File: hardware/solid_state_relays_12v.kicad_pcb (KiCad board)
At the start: 2 copper layers, 100 x 90 mm, 86 parts, among them J1 1190297, J2 1190297, J3 1190297, J4 1190297, J5 1190297, J6 1190297, J7 1190297, J8 1190297, Q1 IRF4905PBF, Q2 IRF4905PBF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

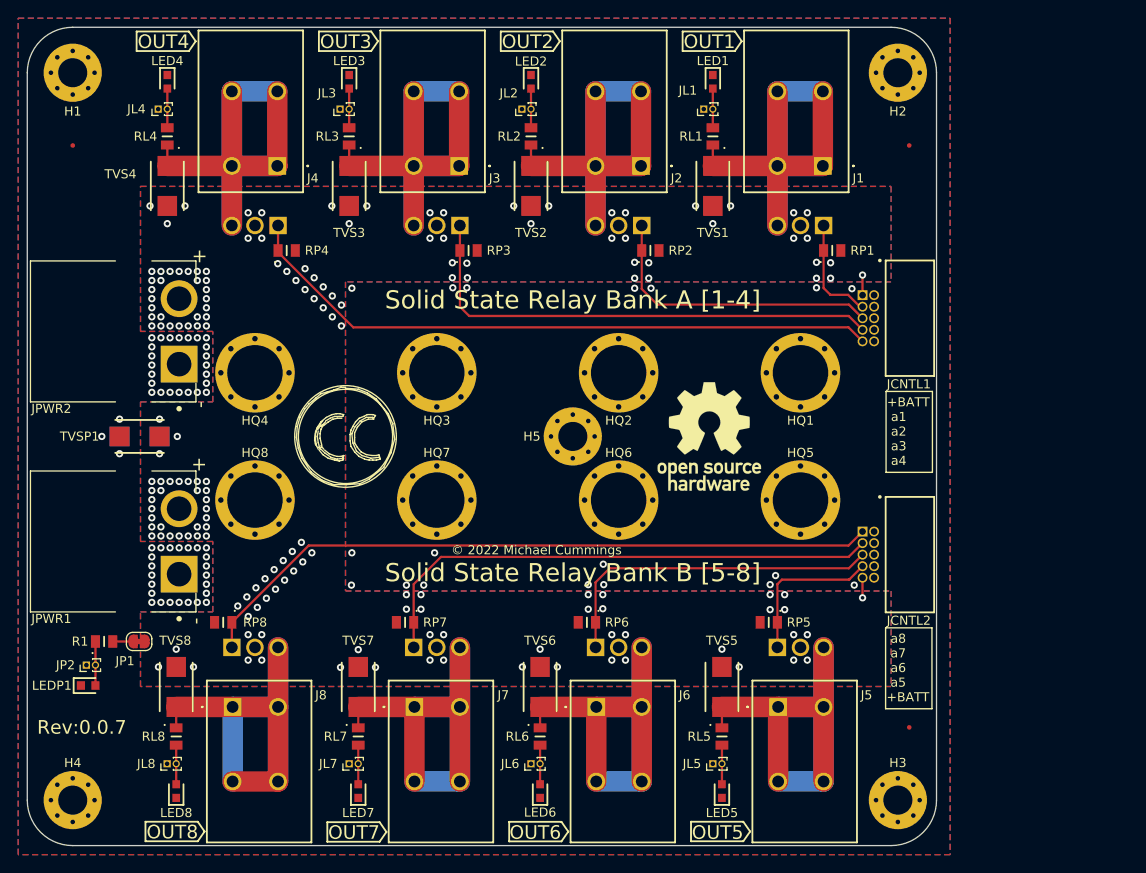
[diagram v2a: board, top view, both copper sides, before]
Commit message: Misc updates mostly related to Silkscreen and adding draft production output
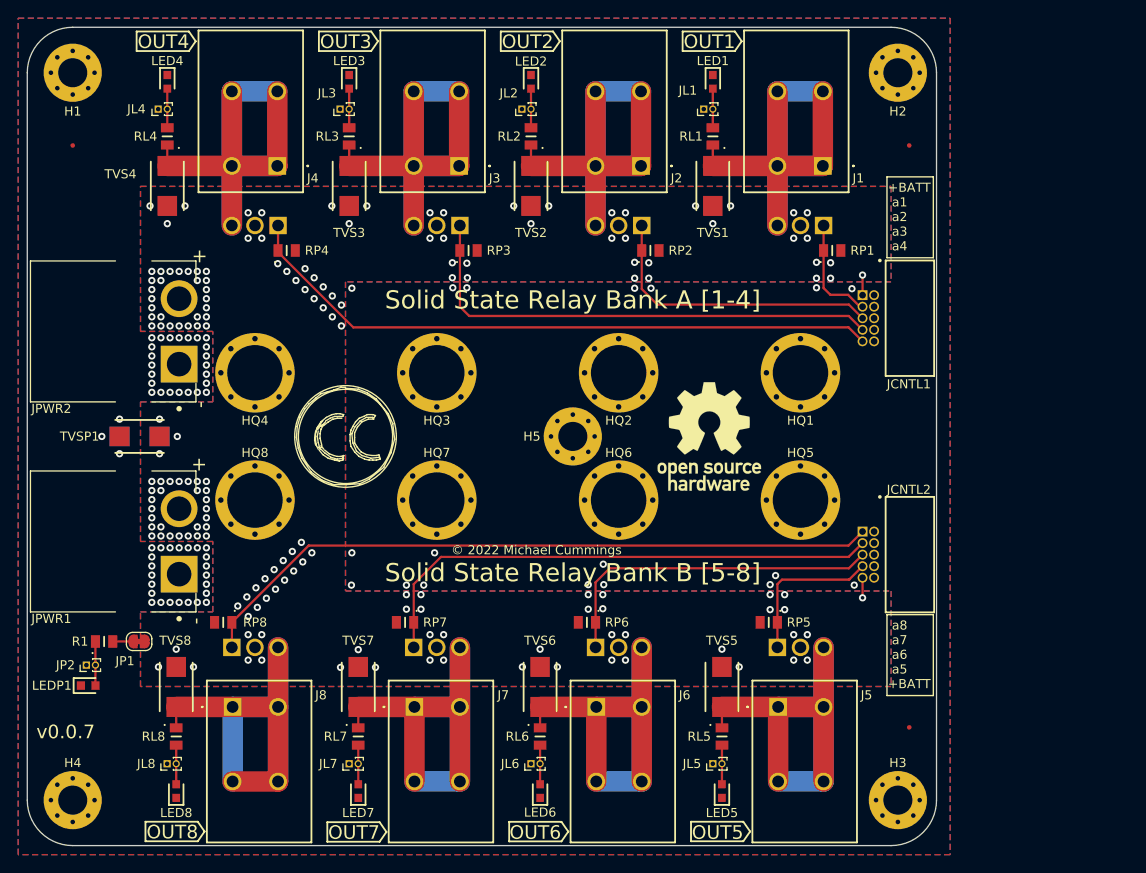
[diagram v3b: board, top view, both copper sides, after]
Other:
- board text added: "v0.0.7"
- board text removed: "Rev:0.0.7"
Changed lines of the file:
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@@
   (title_block
     (title "Solid State Relays 12V")
-    (date "2022-12-22")
+    (date "2023-01-04")
     (rev "0.0.7")
     (comment 2 "creativecommons.org/licenses/by/4.0/")
@@
       (viasonmask false)
       (mode 1)
-      (useauxorigin false)
+      (useauxorigin true)
       (hpglpennumber 1)
       (hpglpenspeed 20)
@@
       (outputformat 1)
       (mirror false)
-      (drillshape 1)
+      (drillshape 0)
       (scaleselection 1)
-      (outputdirectory "")
+      (outputdirectory "C:/repos/github/Dragonrun1/dragon_mobile/solid_state_relays/solid_state_relays_12v/production/")
     )
   )
@@
     (property "Sheetname" "")
     (attr through_hole)
-    (fp_text reference "JCNTL2" (at 7.25 -4.45 180) (layer "F.SilkS")
+    (fp_text reference "JCNTL2" (at -7.15 -4.45 180) (layer "F.SilkS")
       (effects (font (size 1 1) (thickness 0.15)))
     )
@@
       (effects (font (size 1 1) (thickness 0.15)))
     )
-    (fp_text user "${REFERENCE}" (at 7.25 -4.4 180) (layer "B.SilkS")
+    (fp_text user "${REFERENCE}" (at -7.15 -4.4 180) (layer "B.SilkS")
       (effects (font (size 1 1) (thickness 0.15)) (justify mirror))
     )
@@
   (gr_line (start 33.525 16.5375) (end 32.775 17.6125) (layer "F.SilkS") (width 0.2))
   (gr_line (start 32.775 15.4625) (end 33.525 16.5375) (layer "F.SilkS") (width 0.2))
-  (gr_rect (start 109.45 55.05) (end 114.55 63.95) (layer "F.SilkS") (width 0.15) (fill none))
+  (gr_rect (start 109.55 31.45) (end 114.65 40.35) (layer "F.SilkS") (width 0.15) (fill none))
   (gr_line (start 48 102.425) (end 53.75 102.425) (layer "F.SilkS") (width 0.2))
   (gr_line (start 87.075 15.4625) (end 87.075 17.6125) (layer "F.SilkS") (width 0.2))
@@
   (gr_line (start 88 102.375) (end 93.75 102.375) (layer "F.SilkS") (width 0.2))
   (gr_line (start 33.75 104.525) (end 28 104.525) (layer "F.SilkS") (width 0.2))
-  (gr_rect (start 109.4 81.05) (end 114.5 89.95) (layer "F.SilkS") (width 0.15) (fill none))
+  (gr_rect (start 109.55 79.6) (end 114.65 88.5) (layer "F.SilkS") (width 0.15) (fill none))
   (gr_line (start 67.075 15.4625) (end 67.075 17.6125) (layer "F.SilkS") (width 0.2))
   (gr_line (start 27.025 15.4625) (end 32.775 15.4625) (layer "F.SilkS") (width 0.2))
@@
   (gr_line (start 20 15) (end 110 15) (layer "User.9") (width 0.025))
   (gr_arc (start 15 20) (mid 16.464466 16.464466) (end 20 15) (layer "User.9") (width 0.025))
-  (gr_line (start 39.55 64) (end 39.55 70) (layer "User.9") (width 0.15))
+  (gr_line (start 40.04 64) (end 40.04 70) (layer "User.9") (width 0.15))
   (gr_line (start 100.05 50) (end 100.05 56) (layer "User.9") (width 0.15))
   (gr_line (start 60.05 50) (end 60.05 56) (layer "User.9") (width 0.15))
@@
   (gr_line (start 97.05 53) (end 103.05 53) (layer "User.9") (width 0.15))
   (gr_circle (center 80.05 53) (end 83.05 53) (layer "User.9") (width 0.15) (fill none))
-  (gr_line (start 59.55 64) (end 59.55 70) (layer "User.9") (width 0.15))
+  (gr_line (start 60.05 64.05) (end 60.05 70.05) (layer "User.9") (width 0.15))
   (gr_line (start 73.5 60) (end 76.5 60) (layer "User.9") (width 0.15))
-  (gr_circle (center 79.55 67) (end 82.55 67) (layer "User.9") (width 0.15) (fill none))
+  (gr_circle (center 80.04 67) (end 83.04 67) (layer "User.9") (width 0.15) (fill none))
   (gr_circle (center 40.05 53) (end 43.05 53) (layer "User.9") (width 0.15) (fill none))
-  (gr_line (start 56.55 67) (end 62.55 67) (layer "User.9") (width 0.15))
-  (gr_circle (center 99.55 67) (end 102.55 67) (layer "User.9") (width 0.15) (fill none))
+  (gr_line (start 57.05 67.05) (end 63.05 67.05) (layer "User.9") (width 0.15))
+  (gr_circle (center 100.04 67) (end 103.04 67) (layer "User.9") (width 0.15) (fill none))
   (gr_circle (center 110.75 100) (end 110.75 101.5) (layer "User.9") (width 0.15) (fill none))
   (gr_circle (center 110.75 20) (end 110.75 21.5) (layer "User.9") (width 0.15) (fill none))
@@
   (gr_line (start 20 98.5) (end 20 101.5) (layer "User.9") (width 0.15))
   (gr_line (start 18.5 20) (end 21.5 20) (layer "User.9") (width 0.15))
-  (gr_line (start 36.55 67) (end 42.55 67) (layer "User.9") (width 0.15))
-  (gr_line (start 96.55 67) (end 102.55 67) (layer "User.9") (width 0.15))
+  (gr_line (start 37.04 67) (end 43.04 67) (layer "User.9") (width 0.15))
+  (gr_line (start 97.04 67) (end 103.04 67) (layer "User.9") (width 0.15))
   (gr_line (start 115 20) (end 115 100) (layer "User.9") (width 0.025))
-  (gr_circle (center 39.55 67) (end 42.55 67) (layer "User.9") (width 0.15) (fill none))
+  (gr_circle (center 40.04 67) (end 43.04 67) (layer "User.9") (width 0.15) (fill none))
   (gr_circle (center 20 100) (end 20 101.5) (layer "User.9") (width 0.15) (fill none))
-  (gr_circle (center 59.55 67) (end 62.55 67) (layer "User.9") (width 0.15) (fill none))
+  (gr_circle (center 60.05 67.05) (end 63.05 67.05) (layer "User.9") (width 0.15) (fill none))
   (gr_line (start 15 100) (end 15 20) (layer "User.9") (width 0.025))
   (gr_arc (start 115 100) (mid 113.535534 103.535534) (end 110 105) (layer "User.9") (width 0.025))
-  (gr_line (start 76.55 67) (end 82.55 67) (layer "User.9") (width 0.15))
-  (gr_line (start 99.55 64) (end 99.55 70) (layer "User.9") (width 0.15))
+  (gr_line (start 77.04 67) (end 83.04 67) (layer "User.9") (width 0.15))
+  (gr_line (start 100.04 64) (end 100.04 70) (layer "User.9") (width 0.15))
   (gr_line (start 20 18.5) (end 20 21.5) (layer "User.9") (width 0.15))
   (gr_line (start 77.05 53) (end 83.05 53) (layer "User.9") (width 0.15))
-  (gr_line (start 79.55 64) (end 79.55 70) (layer "User.9") (width 0.15))
+  (gr_line (start 80.04 64) (end 80.04 70) (layer "User.9") (width 0.15))
   (gr_circle (center 100.05 53) (end 103.05 53) (layer "User.9") (width 0.15) (fill none))
   (gr_text "JPWR2" (at 17.65 56.95) (layer "B.SilkS")
@@
   )
   (gr_text "6" (at 44 60) (layer "B.SilkS")
-    (effects (font (size 4 4) (thickness 0.5)) (justify left mirror))
+    (effects (font (size 3.5 3.5) (thickness 0.5)) (justify left mirror))
   )
   (gr_text "JPWR1" (at 17.65 80.05) (layer "B.SilkS")
@@
     (effects (font (size 2 2) (thickness 0.3)))
   )
-  (gr_text "Rev:0.0.7" (at 21 92) (layer "F.SilkS")
-    (effects (font (size 1.5 1.5) (thickness 0.25)))
+  (gr_text "v0.0.7" (at 16 92.5) (layer "F.SilkS")
+    (effects (font (size 1.5 1.5) (thickness 0.25)) (justify left))
   )
-  (gr_text "+BATT\n a1\n a2\n a3\n a4" (at 109.55 59.45) (layer "F.SilkS")
+  (gr_text "+BATT\n a1\n a2\n a3\n a4" (at 109.65 35.85) (layer "F.SilkS")
     (effects (font (size 1 1) (thickness 0.15)) (justify left))
   )
@@
     (effects (font (size 1.5 1.5) (thickness 0.2)))
   )
-  (gr_text " a8\n a7\n a6\n a5\n+BATT" (at 109.5 85.45) (layer "F.SilkS")
+  (gr_text " a8\n a7\n a6\n a5\n+BATT" (at 109.65 84) (layer "F.SilkS")
     (effects (font (size 1 1) (thickness 0.15)) (justify left))
   )
@@
     (effects (font (size 2 2) (thickness 0.15)))
   )
+  (dimension (type aligned) (layer "Dwgs.User")
+    (pts (xy 15 100) (xy 115 100))
+    (height 9.95)
+    (gr_text "100 mm" (at 65 108.8) (layer "Dwgs.User")
+      (effects (font (size 1 1) (thickness 0.15)))
+    )
+    (format (units 3) (units_format 1) (precision 4) suppress_zeroes)
+    (style (thickness 0.15) (arrow_length 1.27) (text_position_mode 0) (extension_height 0.58642) (extension_offset 0.5) keep_text_aligned)
+  )
+  (dimension (type aligned) (layer "Dwgs.User")
+    (pts (xy 110 15) (xy 110 105))
+    (height -9.95)
+    (gr_text "90 mm" (at 118.8 60 90) (layer "Dwgs.User")
+      (effects (font (size 1 1) (thickness 0.15)))
+    )
+    (format (units 3) (units_format 1) (precision 4) suppress_zeroes)
+    (style (thickness 0.15) (arrow_length 1.27) (text_position_mode 0) (extension_height 0.58642) (extension_offset 0.5) keep_text_aligned)
+  )
   (via (at 29.7 72.25) (size 0.8) (drill 0.4) (layers "F.Cu" "B.Cu") (free) (net 1))
   (via (at 33.7 55.15) (size 0.8) (drill 0.4) (layers "F.Cu" "B.Cu") (free) (net 1))
@@
     )
   )
+  (group "" (id 266a8590-eeb6-4dec-9efb-d92da2ae7c4b)
+    (members
+      28cb9694-7fef-4c62-aa59-4cb0aa554ed3
+      6b5401cd-6f3d-46b0-bdf2-89b8560c2890
+    )
+  )
   (group "" (id 2854fb29-e996-48a0-88b6-e610dc0a16c0)
     (members
@@
     )
   )
+  (group "" (id 4bb1b916-0d96-40d8-89b8-b660b50127bb)
+    (members
+      100adfdf-b61d-4c4e-bc07-1d7c61bc5bba
+      cb7acb33-cebf-4054-9dc0-88df4033b029
+    )
+  )
   (group "" (id 4d66fdc3-2cab-4109-9d78-7565cedb914a)
     (members
@@
     )
   )
+  (group "" (id d6fce372-540d-4904-b358-628af0bba275)
+    (members
+      24247505-a144-47fa-aa3e-131a3cddf6c7
+      fc58fd49-9bdb-44e3-b7eb-5e9fc8c1fd82
+    )
+  )

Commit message: Make some corections and additions to Mounting.Template layer
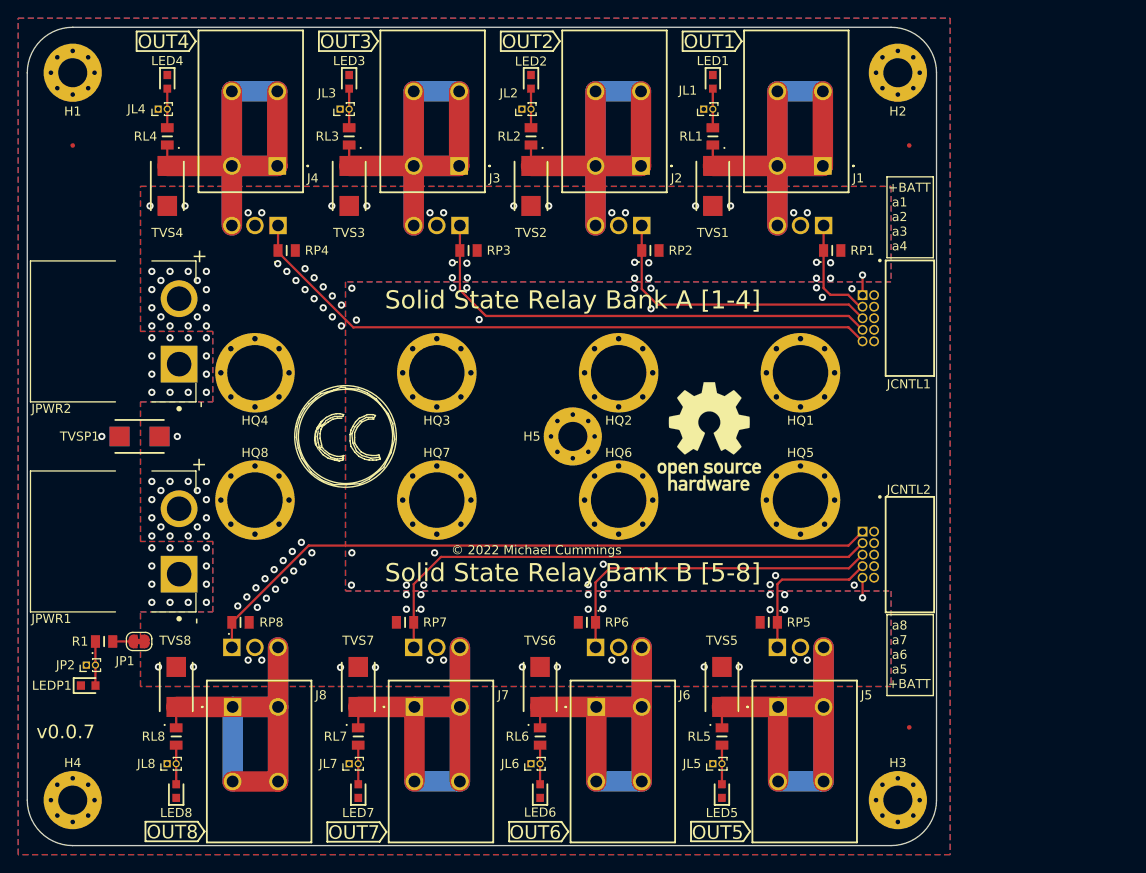
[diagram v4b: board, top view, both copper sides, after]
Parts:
- moved RP8 1.90 mm to (38.5, 80.5), turned to 0 degrees
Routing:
- net /a3: track 54.3 -> 53.2 mm
- net GNDPWR: vias 69 -> 47
- net +BATT: vias 169 -> 119
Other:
- board text added: "H1"
- board text added: "H2"
- board text added: "H3"
- board text added: "H4"
- board text added: "H5"
- board text added: "HQ1"
- board text added: "HQ2"
- board text added: "HQ3"
- board text added: "HQ4"
- board text added: "HQ5"
- board text added: "HQ6"
- board text added: "HQ7"
- board text added: "HQ8"
- board text removed: "HQ1-4 Access Holes"
- board text removed: "HQ5-8 Access Holes"
- board text removed: "Mounting Holes H1-2"
- board text removed: "Mounting Holes H3-4"

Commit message: Updated rev. to v0.0.8
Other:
- board text added: "Licensed under CERN-OHL-W v2"
- board text added: "v0.0.8"
- board text removed: "v0.0.7"

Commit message: Updated production files for v0.0.9
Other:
- board text added: "v0.0.9"
- board text removed: "v0.0.8"
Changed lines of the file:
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@@
     (title "Solid State Relays 12V")
     (date "2023-01-10")
-    (rev "0.0.8")
+    (rev "0.0.9")
     (comment 2 "creativecommons.org/licenses/by/4.0/")
     (comment 3 "License: CC By 4.0")
@@
     (effects (font (size 2 2) (thickness 0.3)))
   )
-  (gr_text "v0.0.8" (at 16 92.5) (layer "F.SilkS")
+  (gr_text "v0.0.9" (at 16 92.5) (layer "F.SilkS")
     (effects (font (size 1.5 1.5) (thickness 0.25)) (justify left))
   )

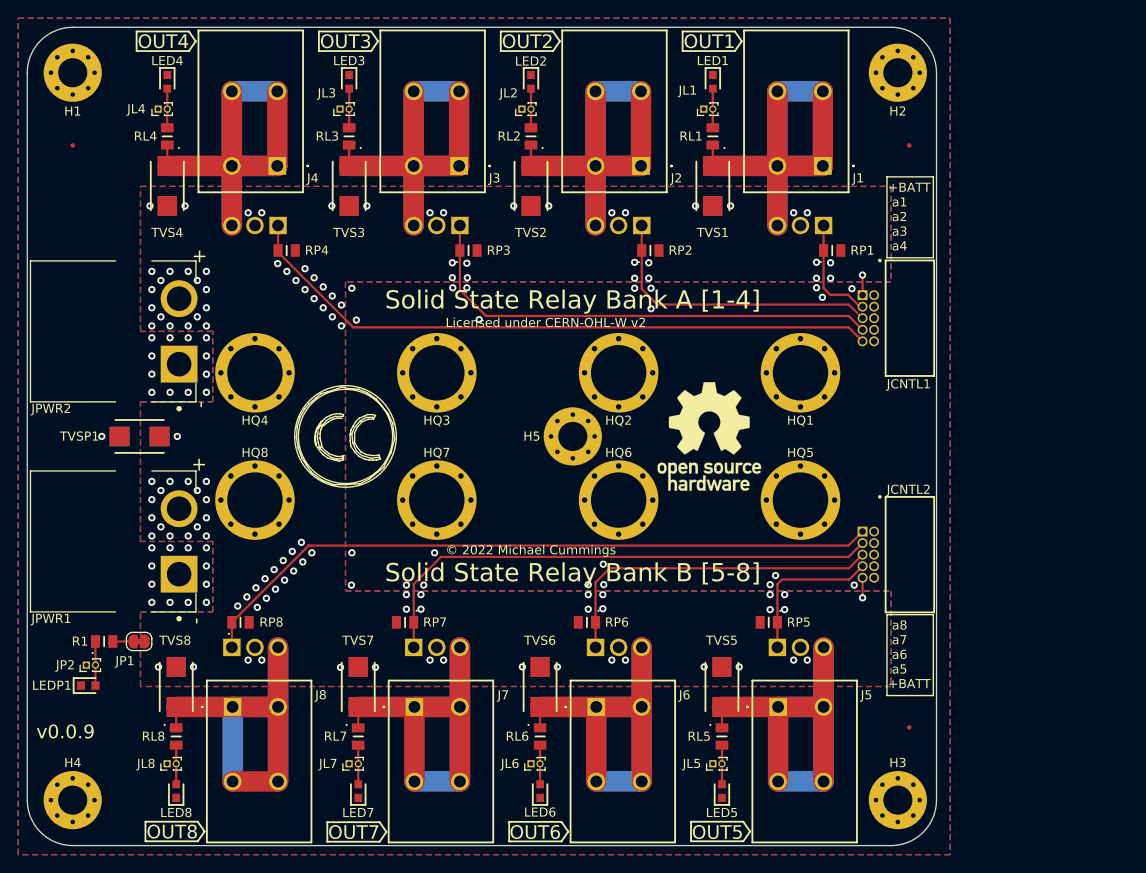
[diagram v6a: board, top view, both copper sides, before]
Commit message: Added power header pins for fans
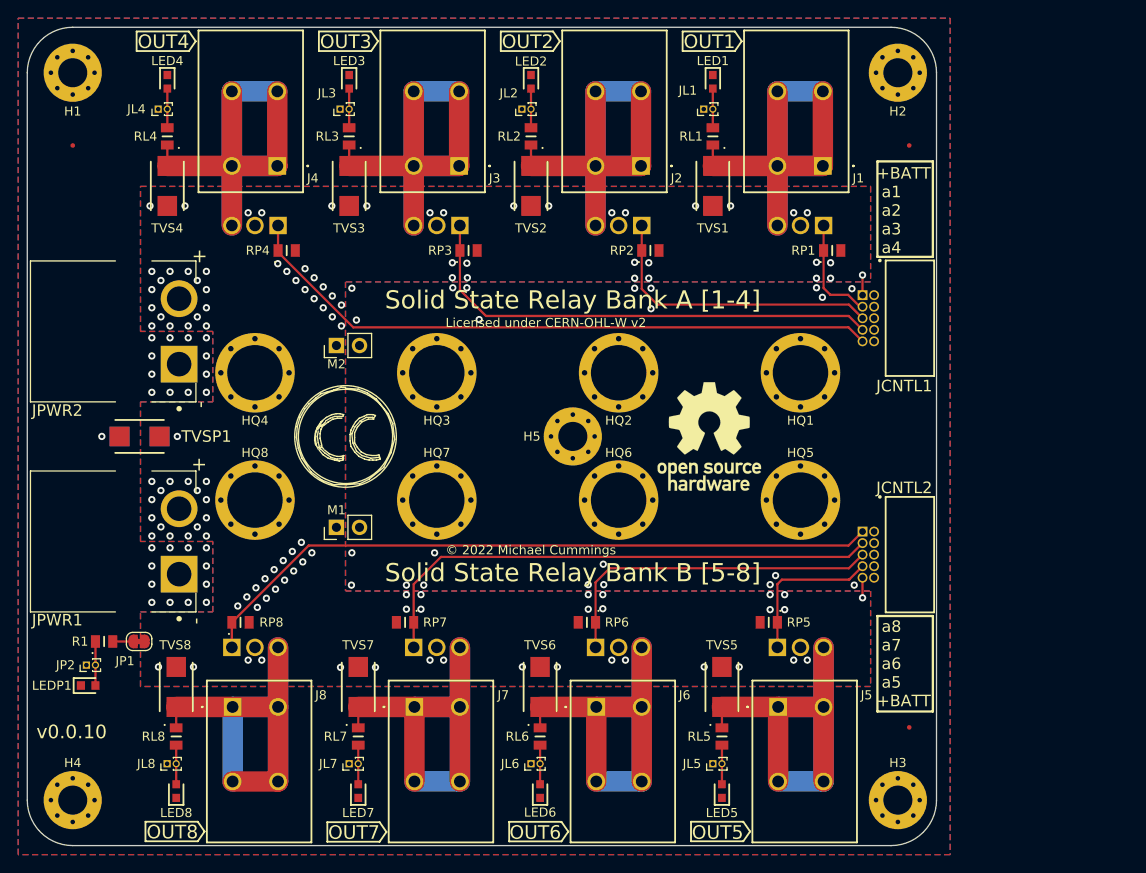
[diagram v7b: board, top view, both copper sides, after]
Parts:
- added M1: Fan, Connector_PinHeader_2.54mm:PinHeader_1x02_P2.54mm_Vertical, F.Cu at (49.0, 70.0)
- added M2: Fan, Connector_PinHeader_2.54mm:PinHeader_1x02_P2.54mm_Vertical, F.Cu at (49.0, 50.0)
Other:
- board text added: "v0.0.10"
- board text removed: "v0.0.9"
